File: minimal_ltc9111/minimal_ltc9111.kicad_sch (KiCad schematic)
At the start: 24 parts, among them Q1 100 V, Q2 100 V, Q3 100 V, Q4 100.0 V, U1 LTC9111RDE-PBF

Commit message: Backup
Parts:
- added J1, J2: FW-02-03-G-D-085-155, connector_footprints:FW-02-03-G-D-085-155, symbol UNITED_CONNECTORS_DATA_BASE:J_FW-02-03-G-D-085-155
- added MB1, MB2: mouse-bite-midle-50mil-200mil, mouse_bite_footprints:mouse-bite-midle-50mil-200mil, symbol UNITED_MOUSE_BITES_DATA_BASE:mouse-bite-midle-50mil-200mil
- added TP1, TP2, TP3, TP4: TestPoint, test_point_footprints:TestPoint_THTPad_Castelated, symbol UNITED_TEST_POINTS:TestPoint_Castelated
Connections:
- net GND: now also J2.2, J2.4, TP4.1
- net OUT: now also J2.1, J2.3, TP3.1
- net POWER_IN_N: now reaches L1.2
- net POWER_IN_N: now also J1.2, J1.4, TP2.1
- net POWER_IN_P: now reaches L1.3
- net POWER_IN_P: now also J1.1, J1.3, TP1.1

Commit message: Backup
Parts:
- C6, C8: footprint capacitor_footprints:C_1210_3225Metric -> capacitor_footprints:C_1210_200_3225Metric; 3dviewer Link (none) -> https://3dviewer.net/index.html#model=https://github.com/io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; Capacitor Type (none) -> Ceramic; Case Code - in 1210 -> 1210_200
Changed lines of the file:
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@@
 			)
 		)
-		(property "Footprint" "capacitor_footprints:C_1210_3225Metric"
+		(property "Footprint" "capacitor_footprints:C_1210_200_3225Metric"
 			(at 261.62 109.22 0)
 			(show_name yes)
@@
 			)
 		)
-		(property "Description" "CAP SMD 4.7 µF X7S 10% 1210 100V"
+		(property "Description" "CAP SMD 4.7 µF X7S 10% 1210_200 100V"
 			(at 256.54 109.22 0)
 			(show_name yes)
@@
 			)
 		)
-		(property "Case Code - in" "1210"
+		(property "Case Code - in" "1210_200"
 			(at 254 109.22 0)
 			(effects
@@
 			)
 		)
+		(property "3dviewer Link" "https://3dviewer.net/index.html#model=https://github.com/ionutms/KiCAD_Symbols_Generator/blob/main/3D_models/C_1210.step"
+			(at 254 109.22 0)
+			(effects
+				(font
+					(size 1.27 1.27)
+				)
+				(justify left)
+				(hide yes)
+			)
+		)
+		(property "Capacitor Type" "Ceramic"
+			(at 251.46 109.22 0)
+			(effects
+				(font
+					(size 1.27 1.27)
+				)
+				(justify left)
+				(hide yes)
+			)
+		)
 		(pin "1"
 		)
@@
 			)
 		)
-		(property "Footprint" "capacitor_footprints:C_1210_3225Metric"
+		(property "Footprint" "capacitor_footprints:C_1210_200_3225Metric"
 			(at 246.38 109.22 0)
 			(show_name yes)
@@
 			)
 		)
-		(property "Description" "CAP SMD 4.7 µF X7S 10% 1210 100V"
+		(property "Description" "CAP SMD 4.7 µF X7S 10% 1210_200 100V"
 			(at 241.3 109.22 0)
 			(show_name yes)
@@
 			)
 		)
-		(property "Case Code - in" "1210"
+		(property "Case Code - in" "1210_200"
 			(at 238.76 109.22 0)
 			(effects
@@
 			(effects
 				(font
+					(size 1.27 1.27)
+				)
+				(justify left)
+				(hide yes)
+			)
+		)
+		(property "3dviewer Link" "https://3dviewer.net/index.html#model=https://github.com/ionutms/KiCAD_Symbols_Generator/blob/main/3D_models/C_1210.step"
+			(at 238.76 109.22 0)
+			(effects
+				(font
+					(size 1.27 1.27)
+				)
+				(justify left)
+				(hide yes)
+			)
+		)
+		(property "Capacitor Type" "Ceramic"
+			(at 236.22 109.22 0)
+			(effects
+				(font

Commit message: Update UUIDs and add 3D viewer link in PCB and schematic files
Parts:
- C1, C5: 3dviewer Link (none) -> https://3dviewer.net/index.html#model=https://github.com/io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
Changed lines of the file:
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@@
+			)
+		)
+		(property "3dviewer Link" "https://3dviewer.net/index.html#model=https://github.com/ionutms/KiCAD_Symbols_Generator/blob/main/3D_models/C_026x026x0236.step"
+			(at 281.94 113.03 0)
+			(effects
+				(font
+					(size 1.27 1.27)
+				)
+				(justify left)
+				(hide yes)
 			)
 		)
@@
 			(effects
 				(font
+					(size 1.27 1.27)
+				)
+				(justify left)
+				(hide yes)
+			)
+		)
+		(property "3dviewer Link" "https://3dviewer.net/index.html#model=https://github.com/ionutms/KiCAD_Symbols_Generator/blob/main/3D_models/C_026x026x0236.step"
+			(at 269.24 113.03 0)
+			(effects
+				(font

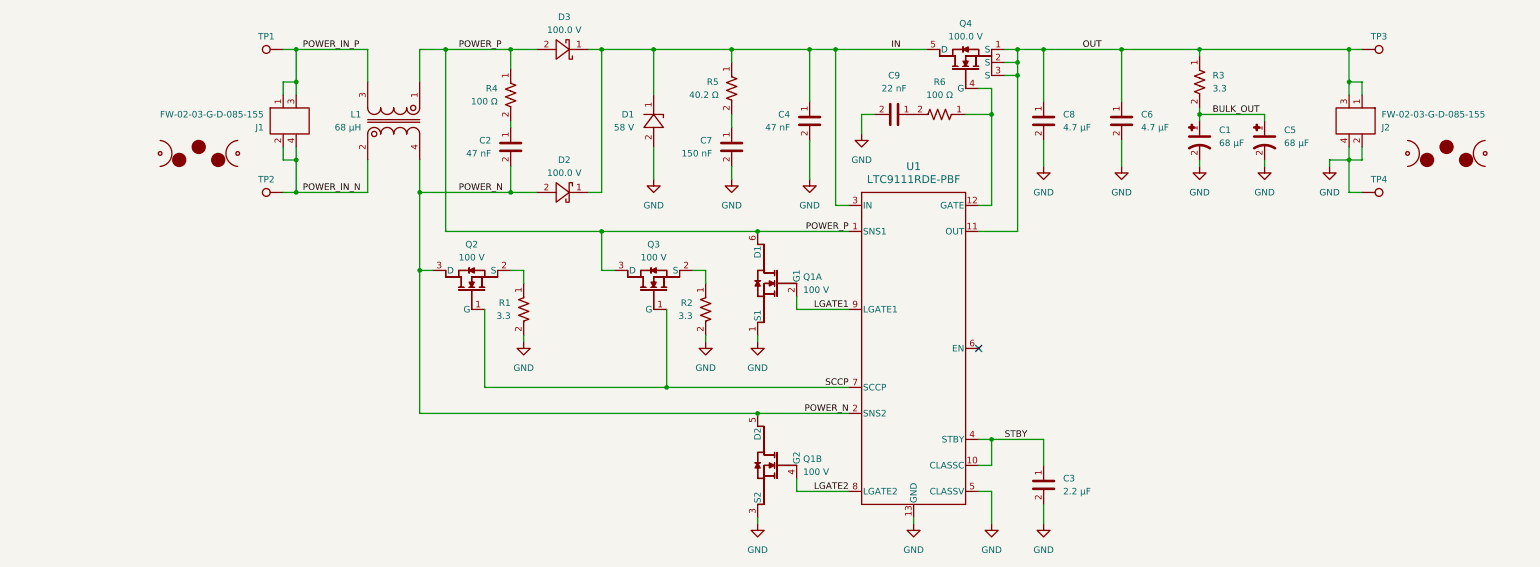
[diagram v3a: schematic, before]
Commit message: Update subproject commit and fix component order in minimal_ltc9111.pdf
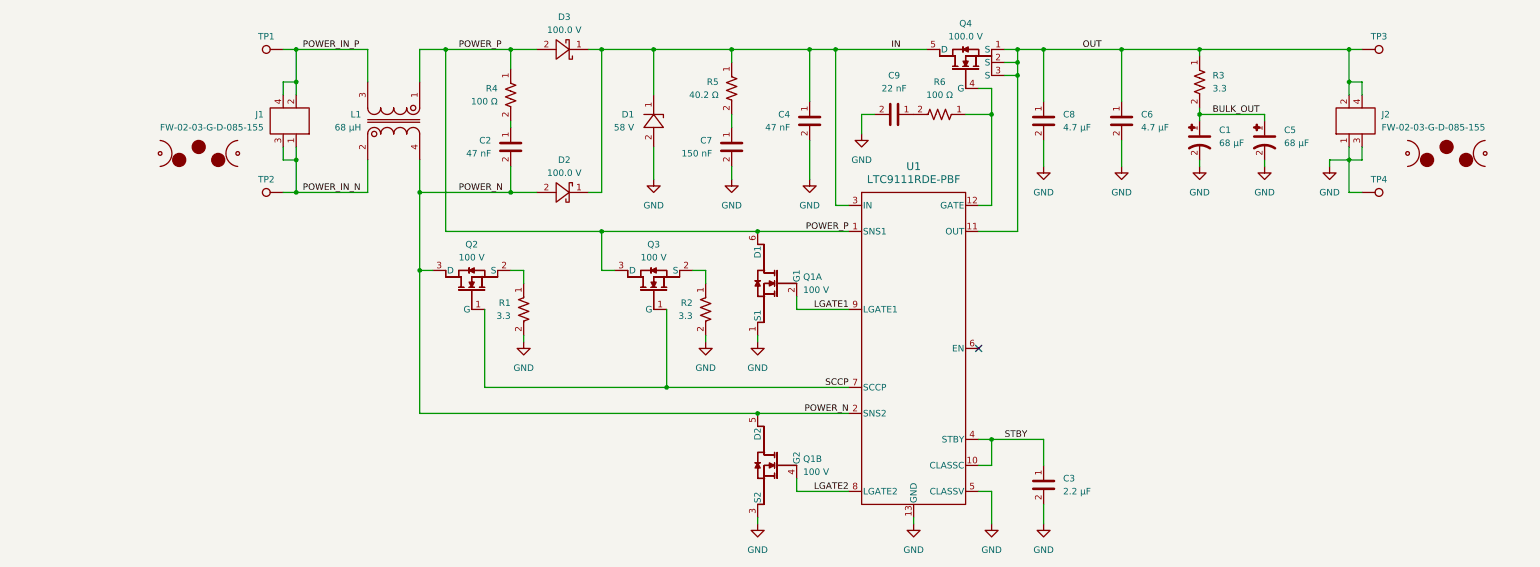
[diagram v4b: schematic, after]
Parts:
- C1, C5: footprint capacitor_footprints:C_026x026x0236_6_6x6_6x6_0Metric -> capacitor_footprints:C_031x0468_8_0x11_9Metric; symbol UNITED_CAPACITORS_DATA_BASE:C_50SVPK68M -> UNITED_CAPACITORS_DATA_BASE:C_50SVPK68M68; 3dviewer Link https://3dviewer.net/index.html#model=https://github.com/ionutms/KiCAD_Symbols_Generator/blob/main/3D_models/C_026x026x0236.step -> https://3dviewer.net/index.html#model=https://github.com/ionutms/KiCAD_Symbols_Generator/blob/main/3D_models/C_031x0468.step; Case Code - in 026x026x0236 -> 031x0468; Case Code - mm 6_6x6_6x6_0 -> 8_0x11_9; MPN 50SVPK68M -> 50SVPK68M68; Series 50SVPK -> 50SVPK68M; Symbol Name C_50SVPK68M -> C_50SVPK68M68; Trustedparts Search https://www.trustedparts.com/en/search/50SVPK68M -> https://www.trustedparts.com/en/search/50SVPK68M68
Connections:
- net GND: now also J2.1, J2.3; no longer J2.2, J2.4
- net OUT: now also J2.2, J2.4; no longer J2.1, J2.3
- net POWER_IN_N: now also J1.1, J1.3; no longer J1.2, J1.4
- net POWER_IN_P: now also J1.2, J1.4; no longer J1.1, J1.3
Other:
- moved on the sheet: J1, J2

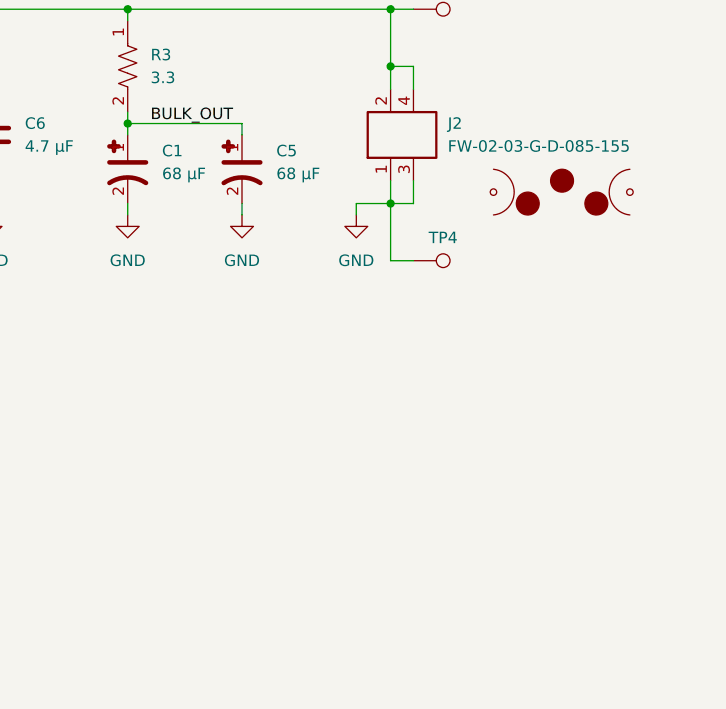
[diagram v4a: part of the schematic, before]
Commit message: Update subproject commit and enhance component blacklist in ibom.config.ini; add new libraries in fp-lib-table and sym-lib-table
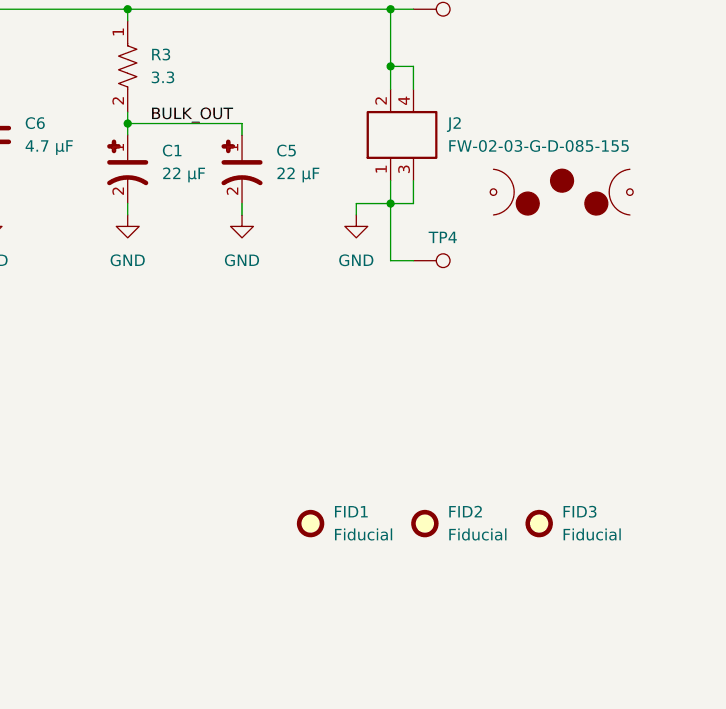
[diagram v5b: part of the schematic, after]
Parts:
- added FID1, FID2, FID3: Fiducial, no_components_footprints:Fiducial_0.5mm_Mask1mm, symbol UNITED_NO_COMPONENTS_DATA_BASE:Fiducial
- C1, C5: value 68 µF -> 22 µF; footprint capacitor_footprints:C_031x0468_8_0x11_9Metric -> capacitor_footprints:C_023x0248_5_9x6_3Metric; symbol UNITED_CAPACITORS_DATA_BASE:C_50SVPK68M68 -> UNITED_CAPACITORS_DATA_BASE:C_50SVPK22M22; 3dviewer Link https://3dviewer.net/index.html#model=https://github.com/ionutms/KiCAD_Symbols_Generator/blob/main/3D_models/C_031x0468.step -> https://3dviewer.net/index.html#model=https://github.com/ionutms/KiCAD_Symbols_Generator/blob/main/3D_models/C_023x0248.step; Case Code - in 031x0468 -> 023x0248; Case Code - mm 8_0x11_9 -> 5_9x6_3; MPN 50SVPK68M68 -> 50SVPK22M22; Series 50SVPK68M -> 50SVPK22M; Symbol Name C_50SVPK68M68 -> C_50SVPK22M22; Trustedparts Search https://www.trustedparts.com/en/search/50SVPK68M68 -> https://www.trustedparts.com/en/search/50SVPK22M22

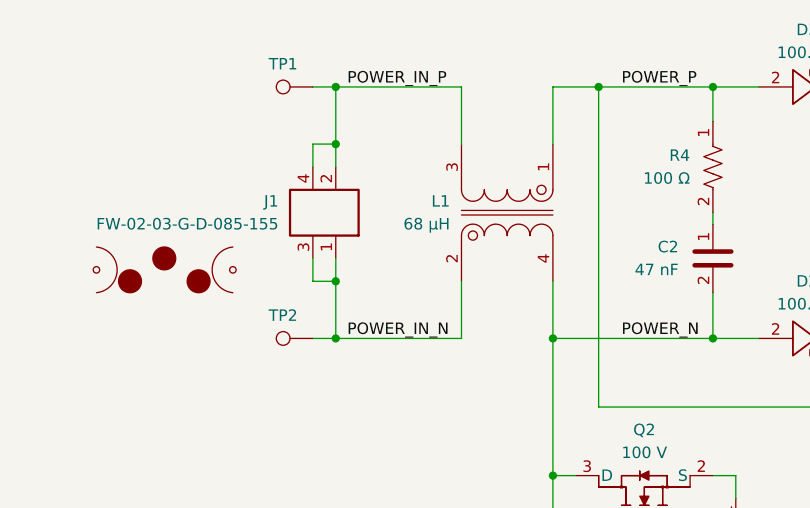
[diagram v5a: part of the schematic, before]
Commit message: Update subproject commit and correct component values in minimal_ltc9111.kicad_sch
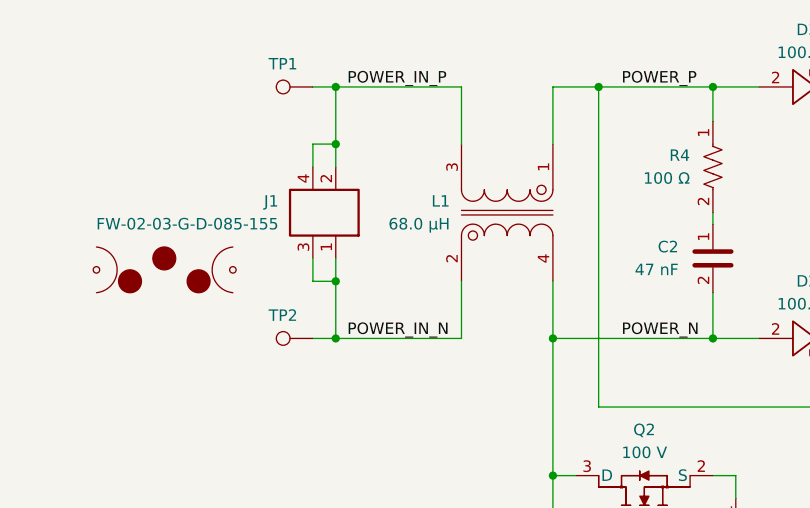
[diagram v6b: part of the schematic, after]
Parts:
- L1: value 68 µH -> 68.0 µH
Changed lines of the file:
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@@
 			)
 		)
-		(property "Value" "68 µH"
+		(property "Value" "68.0 µH"
 			(at 120.65 110.4899 90)
 			(effects
@@
 			)
 		)
-		(property "Description" "COUPLED INDUCTOR SMD 68 µH ±20%"
+		(property "Description" "COUPLED INDUCTOR SMD 68.0 µH ±20%"
 			(at 111.76 109.22 0)
 			(show_name yes)

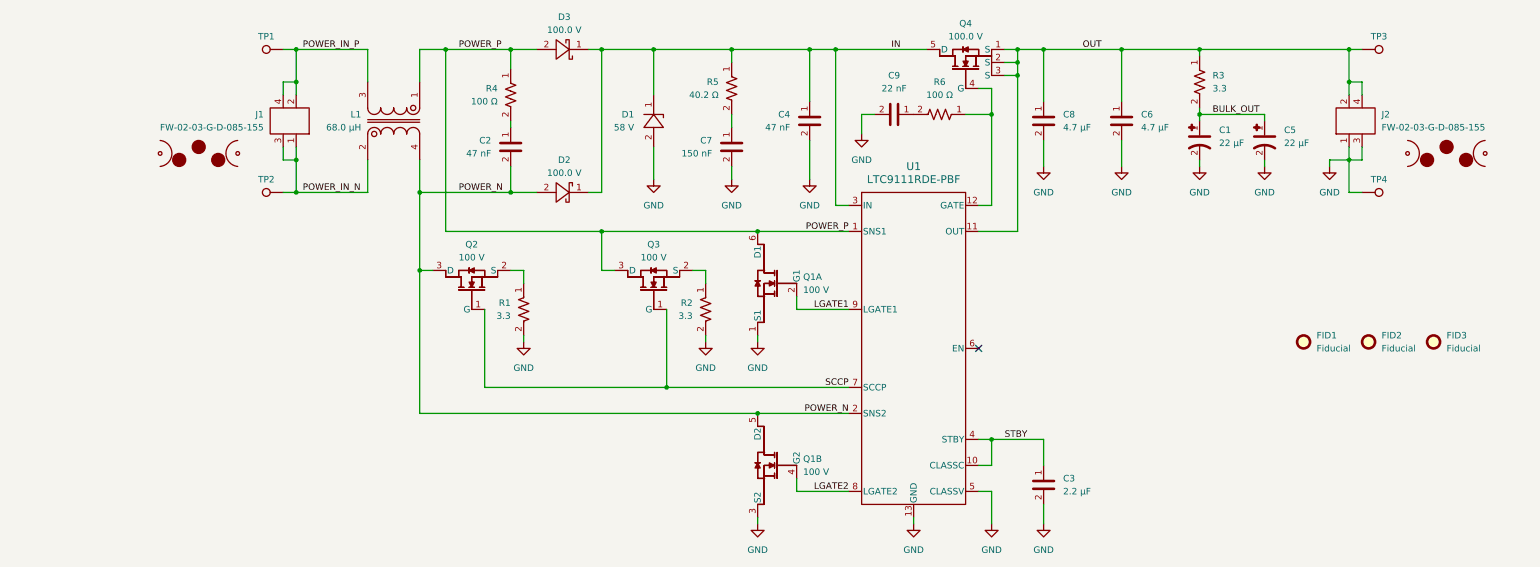
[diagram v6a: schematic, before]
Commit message: Update subproject commit in KiCAD_Symbol_Generator
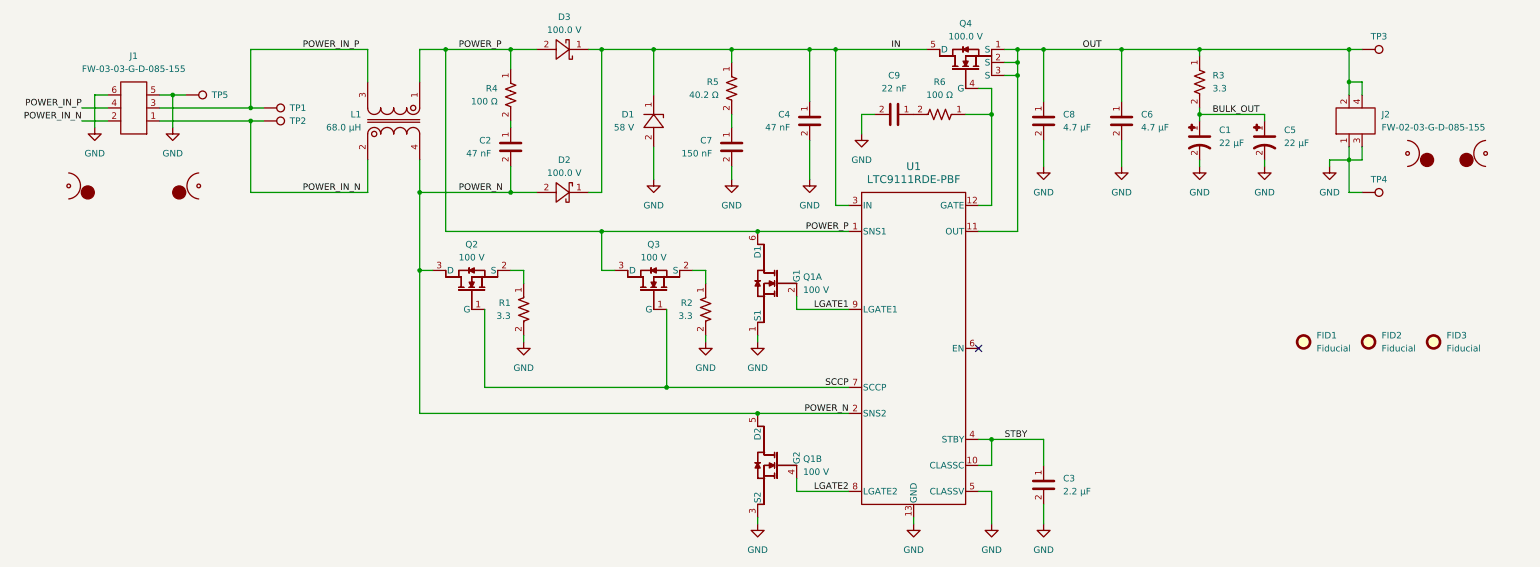
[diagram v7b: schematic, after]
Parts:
- added TP5: TestPoint, test_point_footprints:TestPoint_THTPad_Castelated, symbol UNITED_TEST_POINTS:TestPoint_Castelated
- J1: value FW-02-03-G-D-085-155 -> FW-03-03-G-D-085-155; footprint connector_footprints:FW-02-03-G-D-085-155 -> connector_footprints:FW-03-03-G-D-085-155; symbol UNITED_CONNECTORS_DATA_BASE:J_FW-02-03-G-D-085-155 -> UNITED_CONNECTORS_DATA_BASE:J_FW-03-03-G-D-085-155; MPN FW-02-03-G-D-085-155 -> FW-03-03-G-D-085-155; Pin Count 2 -> 3; Symbol Name J_FW-02-03-G-D-085-155 -> J_FW-03-03-G-D-085-155; Trustedparts Search https://www.trustedparts.com/en/search/FW-02-03-G-D-085-155 -> https://www.trustedparts.com/en/search/FW-03-03-G-D-085-155
- MB1: footprint mouse_bite_footprints:mouse-bite-midle-50mil-200mil -> mouse_bite_footprints:mouse-bite-midle-50mil-250mil; symbol UNITED_MOUSE_BITES_DATA_BASE:mouse-bite-midle-50mil-200mil -> UNITED_MOUSE_BITES_DATA_BASE:mouse-bite-midle-50mil-250mil
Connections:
- net GND: now also J1.5, J1.6, TP5.1
- net POWER_IN_N: now also J1.2; no longer J1.3
- net POWER_IN_P: now also J1.3; no longer J1.2
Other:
- moved on the sheet: TP1, TP2

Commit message: Update footprint library URIs to reference KiCAD_Symbols_Generator
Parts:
- C2, C3, C4, C7, C9: 3dviewer Link (none) -> https://3dviewer.net/index.html#model=https://github.com/io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; Capacitor Type (none) -> Ceramic
- D1: Diode Type TVS -> Unidirectional TVS
- Q1, Q2, Q3, Q4: 3dviewer Link (none) -> https://3dviewer.net/index.html#model=https://github.com/io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
- R1, R2, R3: value 3.3 -> 3.3 Ω; 3dviewer Link (none) -> https://3dviewer.net/index.html#model=https://github.com/io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; Component Type (none) -> Resistor
- R4, R5, R6: 3dviewer Link (none) -> https://3dviewer.net/index.html#model=https://github.com/io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; Component Type (none) -> Resistor
